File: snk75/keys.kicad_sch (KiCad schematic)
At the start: 54 parts

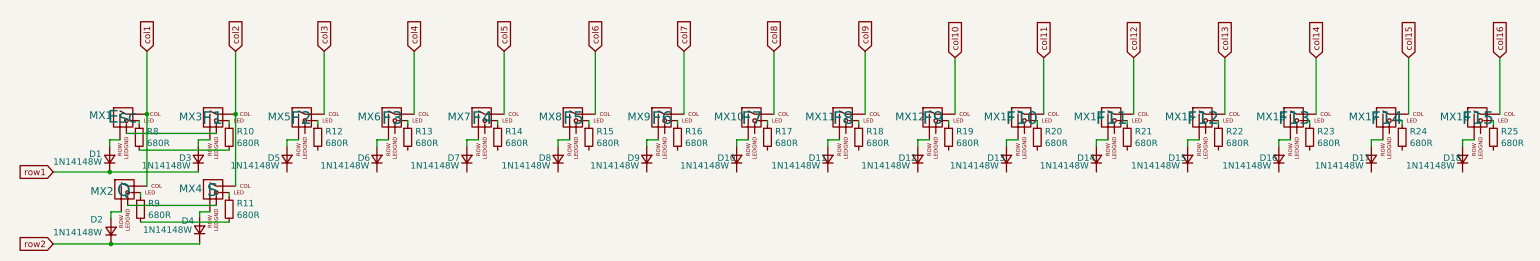
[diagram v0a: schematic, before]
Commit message: feat: keyboard keys
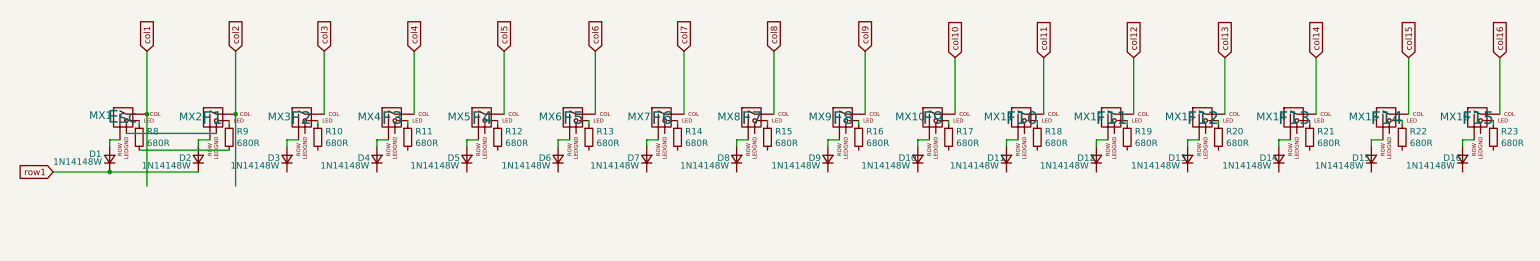
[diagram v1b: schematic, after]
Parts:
- removed D2, D4: 1N14148W, Diode_SMD:D_SOD-123, symbol Device:D_Small
- removed MX2: Q, MX_Only:MXOnly-1U, symbol MX_Alps_Hybrid:MX-LED
- removed MX4: S, MX_Only:MXOnly-1U, symbol MX_Alps_Hybrid:MX-LED
- removed R11, R9: 680R, Resistor_SMD:R_1206_3216Metric_Pad1.30x1.75mm_HandSolder, symbol Device:R_Small
- renumbered D12 to D10, D13 to D11, D14 to D12, D15 to D13, D16 to D14, D17 to D15, D18 to D16, D3 to D2, D5 to D3, D6 to D4, D7 to D5, D8 to D6, D9 to D7, D10 to D8, D11 to D9, MX12 to MX10, MX13 to MX11, MX14 to MX12, MX15 to MX13, MX16 to MX14, MX17 to MX15, MX18 to MX16, MX3 to MX2, MX5 to MX3, MX6 to MX4, MX7 to MX5, MX8 to MX6, MX9 to MX7, MX10 to MX8, MX11 to MX9, R12 to R10, R13 to R11, R14 to R12, R15 to R13, R16 to R14, R17 to R15, R18 to R16, R19 to R17, R20 to R18, R21 to R19, R22 to R20, R23 to R21, R24 to R22, R25 to R23, R10 to R9
